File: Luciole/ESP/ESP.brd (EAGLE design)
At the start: 30 x 30 mm, 9 parts

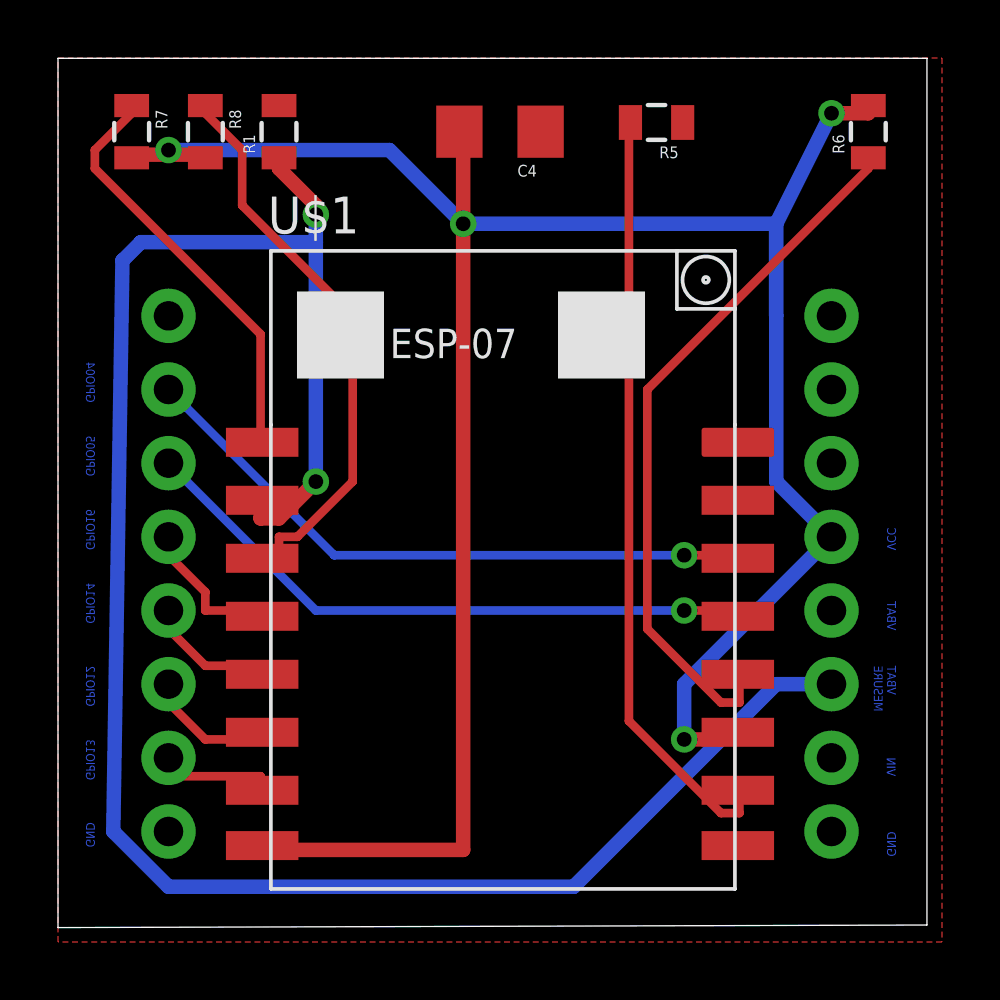
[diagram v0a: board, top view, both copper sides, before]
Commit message: Luciole V1 Ok ; Baballe V1 En cours
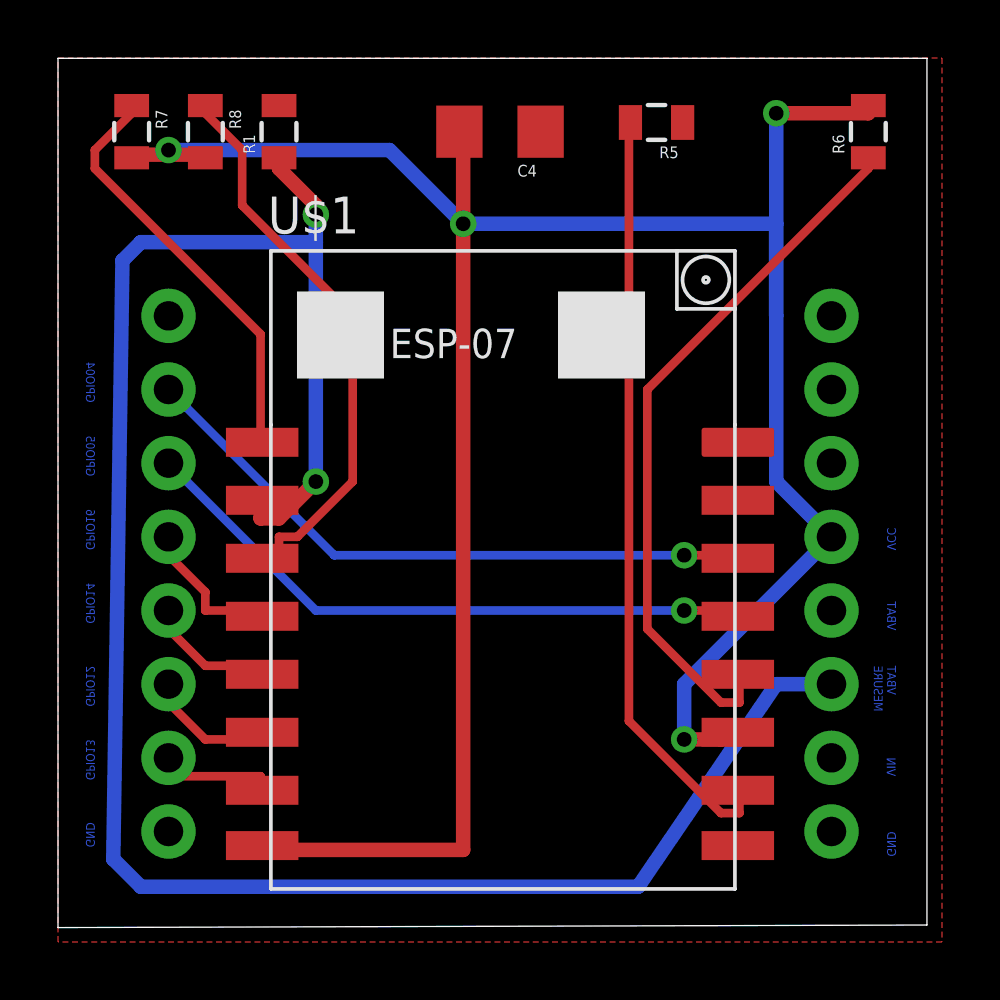
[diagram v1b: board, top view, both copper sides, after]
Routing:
- net VCC: track 85.1 -> 86.6 mm
- net VBAT_MESURE: track 69.9 -> 71.2 mm
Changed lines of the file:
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@@
 <setting verticaltext="up"/>
 </settings>
-<grid distance="12.5" unitdist="mil" unit="mil" style="lines" multiple="1" display="no" altdistance="0.025" altunitdist="inch" altunit="inch"/>
+<grid distance="0.000123031496" unitdist="mil" unit="mil" style="lines" multiple="1" display="no" altdistance="0.025" altunitdist="inch" altunit="inch"/>
 <layers>
 <layer number="1" name="Top" color="4" fill="1" visible="yes" active="yes"/>
@@
 <wire x1="70.601190625" y1="31.74" x2="40.64" y2="31.74" width="0" layer="20"/>
 <wire x1="40.64" y1="31.74" x2="40.64" y2="1.766671875" width="0" layer="20"/>
-<dimension x1="40.64" y1="31.74" x2="70.657375" y2="31.711778125" x3="55.61480625" y3="-4.309225" textsize="1.778" layer="1"/>
-<dimension x1="40.64" y1="31.74" x2="40.627990625" y2="1.678340625" x3="74.90338125" y3="16.695478125" textsize="1.778" layer="1"/>
 <text x="41.91" y="21.2725" size="0.3048" layer="16" font="vector" rot="MR270">GPIO04</text>
 <text x="41.91" y="18.7325" size="0.3048" layer="16" font="vector" rot="MR270">GPIO05</text>
@@
 <text x="69.5325" y="13.0175" size="0.3048" layer="16" font="vector" rot="MR270">VBAT</text>
 <text x="69.5325" y="15.5575" size="0.3048" layer="16" font="vector" rot="MR270">VCC</text>
-<dimension x1="40.64" y1="31.75" x2="40.64" y2="24.13" x3="37.7825" y3="27.94" textsize="0.3048" layer="1"/>
-<dimension x1="40.64" y1="31.75" x2="45.72" y2="31.75" x3="43.18" y3="33.02" textsize="0.3048" layer="1"/>
 </plain>
 <attributes>
@@
 <wire x1="43.18" y1="28.41625" x2="43.18" y2="28.31" width="0.5" layer="1"/>
 <wire x1="45.72" y1="28.41625" x2="45.72" y2="28.31" width="0.5" layer="1"/>
-<wire x1="67.31" y1="29.845" x2="68.58" y2="29.845" width="0.5" layer="1"/>
-<wire x1="65.405" y1="26.035" x2="67.31" y2="29.845" width="0.5" layer="16"/>
+<wire x1="65.405" y1="29.845" x2="68.58" y2="29.845" width="0.5" layer="1"/>
+<wire x1="65.405" y1="26.035" x2="65.405" y2="29.845" width="0.5" layer="16"/>
 <wire x1="65.405" y1="17.145" x2="65.405" y2="22.86" width="0.5" layer="16"/>
 <wire x1="67.31" y1="15.24" x2="65.405" y2="17.145" width="0.5" layer="16"/>
@@
 <wire x1="67.31" y1="15.24" x2="62.23" y2="10.16" width="0.5" layer="16"/>
 <wire x1="63.5" y1="8.255" x2="64.08" y2="8.5" width="0.5" layer="1"/>
-<via x="67.31" y="29.845" extent="1-16" drill="0.508"/>
+<via x="65.405" y="29.845" extent="1-16" drill="0.508"/>
 <via x="54.61" y="26.035" extent="1-16" drill="0.508"/>
 <via x="44.45" y="28.575" extent="1-16" drill="0.508"/>
@@
 <wire x1="47.625" y1="16.51" x2="47.68" y2="16.5" width="0.5" layer="1"/>
 <wire x1="65.405" y1="10.16" x2="67.31" y2="10.16" width="0.5" layer="16"/>
-<wire x1="58.42" y1="3.175" x2="65.405" y2="10.16" width="0.5" layer="16"/>
-<wire x1="44.45" y1="3.175" x2="58.42" y2="3.175" width="0.5" layer="16"/>
-<wire x1="42.545" y1="5.08" x2="44.45" y2="3.175" width="0.5" layer="16"/>
-<wire x1="42.8625" y1="24.765" x2="42.545" y2="5.08" width="0.5" layer="16"/>
+<wire x1="60.6425" y1="3.175" x2="65.405" y2="10.16" width="0.5" layer="16"/>
+<wire x1="43.4975" y1="3.175" x2="60.6425" y2="3.175" width="0.5" layer="16"/>
+<wire x1="42.545" y1="4.1275" x2="43.4975" y2="3.175" width="0.5" layer="16"/>
+<wire x1="42.8625" y1="24.765" x2="42.545" y2="4.1275" width="0.5" layer="16"/>
 <wire x1="43.4975" y1="25.4" x2="42.8625" y2="24.765" width="0.5" layer="16"/>
 <wire x1="49.53" y1="25.4" x2="43.4975" y2="25.4" width="0.5" layer="16"/>
